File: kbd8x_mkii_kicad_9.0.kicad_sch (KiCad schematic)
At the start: 20 parts, among them J1 AVR-ISP-6, SW1 SW_Push, U1 ATmega32U4-A, U2 PRTR5V0U2X, Y1 16MHz

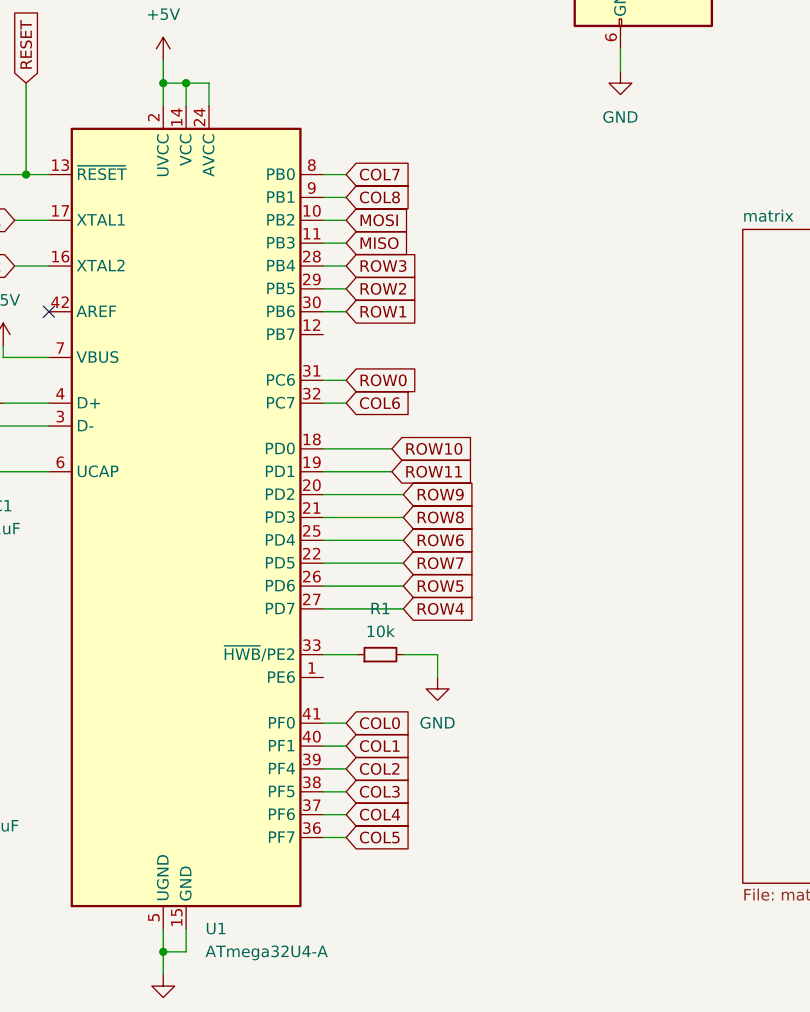
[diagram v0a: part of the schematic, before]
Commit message: Applied row/col on different layers rule to clean up traces, hopefully ready for production.
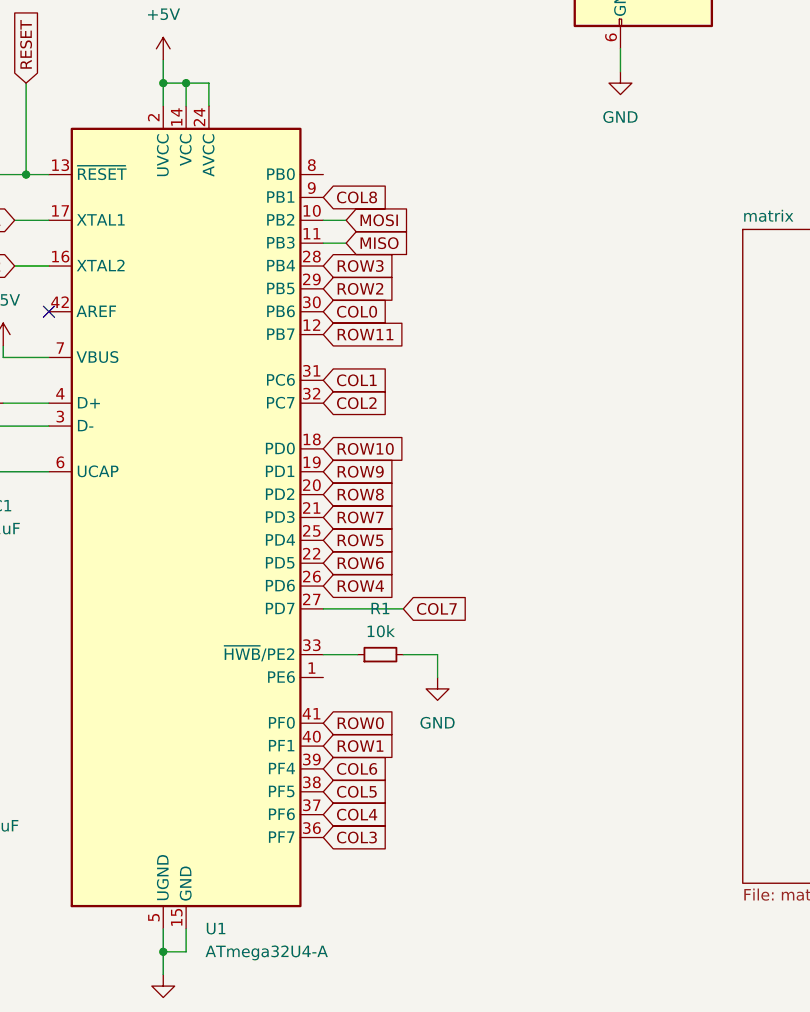
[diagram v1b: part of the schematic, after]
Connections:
- net COL0: now also U1.30 (PB6); no longer U1.41 (PF0)
- net COL1: now also U1.31 (PC6); no longer U1.40 (PF1)
- net COL2: now also U1.32 (PC7); no longer U1.39 (PF4)
- net COL3: now also U1.36 (PF7); no longer U1.38 (PF5)
- net COL5: now also U1.38 (PF5); no longer U1.36 (PF7)
- net COL6: now also U1.39 (PF4); no longer U1.32 (PC7)
- net COL7: now also U1.27 (PD7); no longer U1.8 (PB0)
- net ROW0: now also U1.41 (PF0); no longer U1.31 (PC6)
- net ROW1: now also U1.40 (PF1); no longer U1.30 (PB6)
- net ROW11: now also U1.12 (PB7); no longer U1.19 (PD1)
- net ROW4: now also U1.26 (PD6); no longer U1.27 (PD7)
- net ROW5: now also U1.25 (PD4); no longer U1.26 (PD6)
- net ROW6: now also U1.22 (PD5); no longer U1.25 (PD4)
- net ROW7: now also U1.21 (PD3); no longer U1.22 (PD5)
- net ROW8: now also U1.20 (PD2); no longer U1.21 (PD3)
- net ROW9: now also U1.19 (PD1); no longer U1.20 (PD2)
